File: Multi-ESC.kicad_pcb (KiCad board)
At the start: 2 copper layers, 252 parts, among them J1 Conn_01x01, J10 Conn_01x01, J11 Conn_01x01, J12 Conn_01x01, J13 Conn_01x01, J14 Conn_01x01, J15 Conn_01x01, J16 Conn_01x01, J17 Conn_01x03, J18 Conn_01x05, J2 Conn_01x01, J3 Conn_01x01, J4 Conn_01x01, J5 Conn_01x01, J6 Conn_01x01, J7 Conn_01x01, J8 Conn_01x01, J9 Conn_01x01, Q1 DI030N10PT-AQ, Q10 DI030N10PT-AQ, Q11 DI030N10PT-AQ, Q12 DI030N10PT-AQ, Q13 DI030N10PT-AQ, Q14 Q_PMOS_DGS, Q15 DI030N10PT-AQ, Q16 DI030N10PT-AQ, Q17 DI030N10PT-AQ, Q18 DI030N10PT-AQ, Q19 DI030N10PT-AQ, Q2 DI030N10PT-AQ, Q20 DI030N10PT-AQ, Q21 Q_PMOS_DGS, Q22 DI030N10PT-AQ, Q23 DI030N10PT-AQ, Q24 DI030N10PT-AQ, Q25 DI030N10PT-AQ, Q26 DI030N10PT-AQ, Q27 DI030N10PT-AQ, Q28 Q_PMOS_DGS, Q3 DI030N10PT-AQ, Q4 DI030N10PT-AQ, Q5 DI030N10PT-AQ, Q6 DI030N10PT-AQ, Q7 Q_PMOS_DGS, Q8 DI030N10PT-AQ, Q9 DI030N10PT-AQ, U1 STM32F318K8Ux, U10 DRV8320SR, U11 MIC5504-1.8YM5, U12 STM32F318K8Ux, U13 DRV8320SR, U2 DRV8320SR, U3 LMR51450FN, U4 MIC5504-1.8YM5, U5 MIC5504-1.8YM5, U6 STM32F318K8Ux, U7 DRV8320SR, U8 MIC5504-1.8YM5, U9 STM32F318K8Ux, Y1 8MHz, Y2 8MHz, Y3 8MHz, Y4 8MHz

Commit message: added journal entry
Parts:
- moved C2 5.54 mm to (260.4, 116.5), turned to -90 degrees
- moved C3 3.94 mm to (261.4, 116.5), turned to -90 degrees
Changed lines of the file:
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@@
 	(footprint "Capacitor_SMD:C_0402_1005Metric"
 		(layer "F.Cu")
-		(at 259.18 121.9)
+		(at 260.4 116.5 -90)
 		(descr "Capacitor SMD 0402 (1005 Metric), square (rectangular) end terminal, IPC-7351 nominal, (Body size source: IPC-SM-782 page 76, https://www.pcb-3d.com/wordpress/wp-content/uploads/ipc-sm-782a_amendment_1_and_2.pdf)")
 		(tags "capacitor")
 		(property "Reference" "C2"
-			(at 0 -1.16 0)
+			(at 0 -1.16 90)
 			(layer "F.SilkS")
+			(hide yes)
 			(effects
 				(font
@@
 		)
 		(property "Value" "100nF"
-			(at 0 1.16 0)
+			(at 0 1.16 90)
 			(layer "F.Fab")
 			(effects
@@
 		)
 		(property "Datasheet" ""
-			(at 0 0 0)
+			(at 0 0 90)
 			(layer "F.Fab")
 			(hide yes)
@@
 		)
 		(property "Description" "Unpolarized capacitor"
-			(at 0 0 0)
+			(at 0 0 90)
 			(layer "F.Fab")
 			(hide yes)
@@
 		)
 		(property "KiLib_Generator" "SMD_2terminal_chip_molded"
-			(at 0 0 0)
+			(at 0 0 90)
 			(layer "F.SilkS")
 			(hide yes)
@@
 		)
 		(property "MPN" ""
-			(at 0 0 0)
+			(at 0 0 270)
 			(unlocked yes)
 			(layer "F.Fab")
@@
 		(duplicate_pad_numbers_are_jumpers no)
 		(fp_line
-			(start -0.107836 -0.36)
-			(end 0.107836 -0.36)
+			(start -0.107836 0.36)
+			(end 0.107836 0.36)
 			(stroke
 				(width 0.12)
@@
 		)
 		(fp_line
-			(start -0.107836 0.36)
-			(end 0.107836 0.36)
+			(start -0.107836 -0.36)
+			(end 0.107836 -0.36)
 			(stroke
 				(width 0.12)
@@
 		)
 		(fp_text user "${REFERENCE}"
-			(at 0 0 0)
+			(at 0 0 90)
 			(layer "F.Fab")
 			(effects
@@
 		)
 		(pad "1" smd roundrect
-			(at -0.48 0)
+			(at -0.48 0 270)
 			(size 0.56 0.62)
 			(layers "F.Cu" "F.Mask" "F.Paste")
@@
 		)
 		(pad "2" smd roundrect
-			(at 0.48 0)
+			(at 0.48 0 270)
 			(size 0.56 0.62)
 			(layers "F.Cu" "F.Mask" "F.Paste")
@@
 	(footprint "Capacitor_SMD:C_0402_1005Metric"
 		(layer "F.Cu")
-		(at 259.28 119.8)
+		(at 261.4 116.48 -90)
 		(descr "Capacitor SMD 0402 (1005 Metric), square (rectangular) end terminal, IPC-7351 nominal, (Body size source: IPC-SM-782 page 76, https://www.pcb-3d.com/wordpress/wp-content/uploads/ipc-sm-782a_amendment_1_and_2.pdf)")
 		(tags "capacitor")
 		(property "Reference" "C3"
-			(at 0 -1.16 0)
+			(at 0 -1.16 90)
 			(layer "F.SilkS")
+			(hide yes)
 			(effects
 				(font
@@
 		)
 		(property "Value" "100nF"
-			(at 0 1.16 0)
+			(at 0 1.16 90)
 			(layer "F.Fab")
 			(effects
@@
 		)
 		(property "Datasheet" ""
-			(at 0 0 0)
+			(at 0 0 90)
 			(layer "F.Fab")
 			(hide yes)
@@
 		)
 		(property "Description" "Unpolarized capacitor"
-			(at 0 0 0)
+			(at 0 0 90)
 			(layer "F.Fab")
 			(hide yes)
@@
 		)
 		(property "KiLib_Generator" "SMD_2terminal_chip_molded"
-			(at 0 0 0)
+			(at 0 0 90)
 			(layer "F.SilkS")
 			(hide yes)
@@
 		)
 		(property "MPN" ""
-			(at 0 0 0)
+			(at 0 0 270)
 			(unlocked yes)
 			(layer "F.Fab")
@@
 		(duplicate_pad_numbers_are_jumpers no)
 		(fp_line
-			(start -0.107836 -0.36)
-			(end 0.107836 -0.36)
+			(start -0.107836 0.36)
+			(end 0.107836 0.36)
 			(stroke
 				(width 0.12)
@@
 		)
 		(fp_line
-			(start -0.107836 0.36)
-			(end 0.107836 0.36)
+			(start -0.107836 -0.36)
+			(end 0.107836 -0.36)
 			(stroke
 				(width 0.12)
@@
 		)
 		(fp_text user "${REFERENCE}"
-			(at 0 0 0)
+			(at 0 0 90)
 			(layer "F.Fab")
 			(effects
@@
 		)
 		(pad "1" smd roundrect
-			(at -0.48 0)
+			(at -0.48 0 270)
 			(size 0.56 0.62)
 			(layers "F.Cu" "F.Mask" "F.Paste")
@@
 		)
 		(pad "2" smd roundrect
-			(at 0.48 0)
+			(at 0.48 0 270)
 			(size 0.56 0.62)
 			(layers "F.Cu" "F.Mask" "F.Paste")

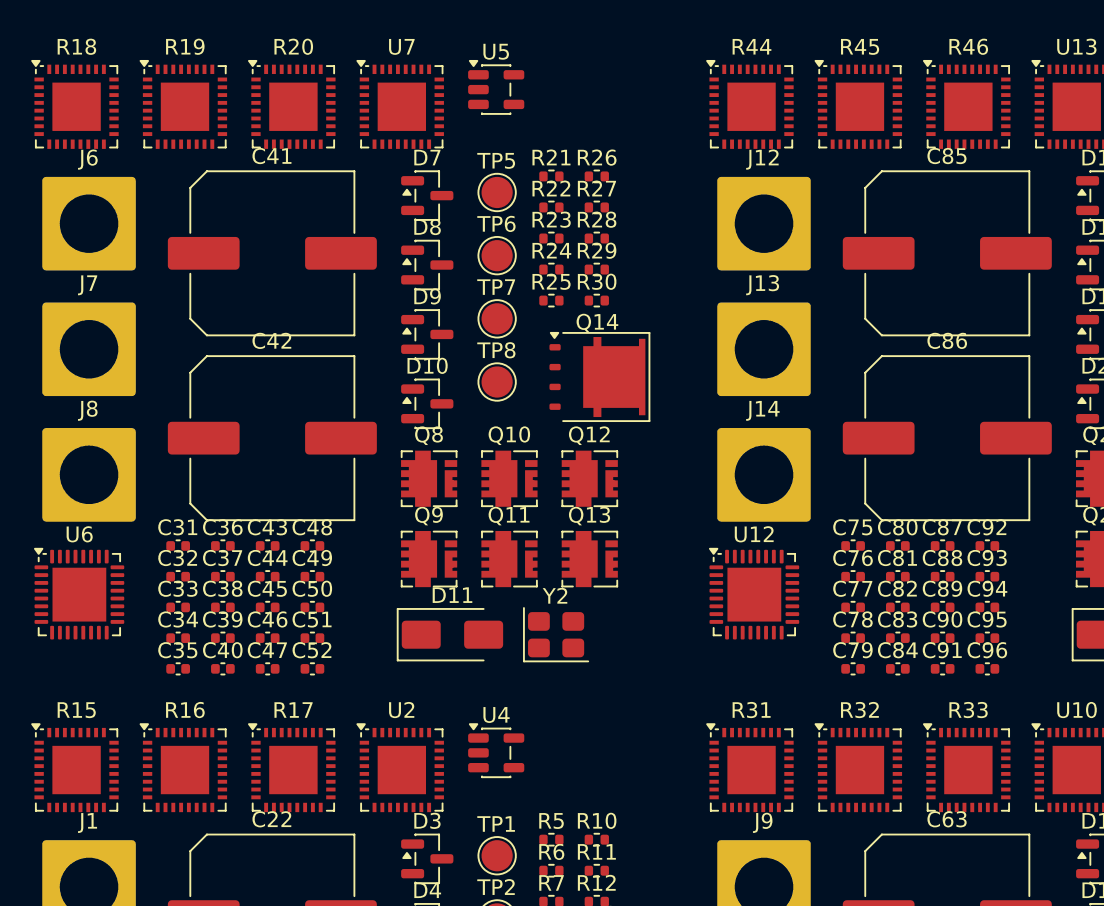
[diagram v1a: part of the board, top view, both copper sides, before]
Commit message: fixed footprints
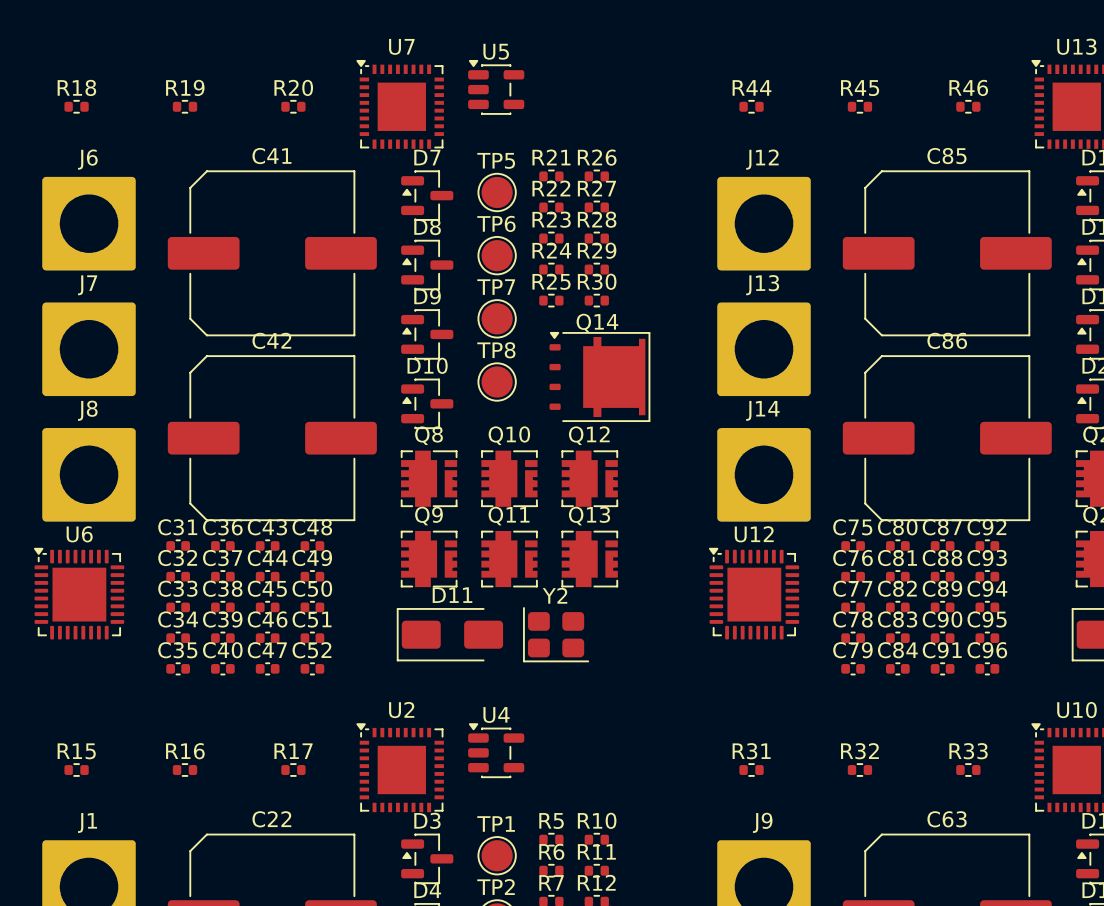
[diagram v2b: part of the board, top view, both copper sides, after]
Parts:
- R15, R16, R17, R18, R19, R20, R31, R32, R33, R44, R45, R46: footprint Package_DFN_QFN:WQFN-32-1EP_5x5mm_P0.5mm_EP3.1x3.1mm -> Resistor_SMD:R_0402_1005Metric

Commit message: set driver layout
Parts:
- removed D20, D3, D5: BAT54C, Package_TO_SOT_SMD:SOT-23
- added D23: BAT54CW, Package_TO_SOT_SMD:SOT-323_SC-70, F.Cu at (-157.3, 34.2)
- added D24: BAT54CW, Package_TO_SOT_SMD:SOT-323_SC-70, F.Cu at (-139.4, 34.2)
- added D25: BAT54CW, Package_TO_SOT_SMD:SOT-323_SC-70, F.Cu at (-145.4, 34.2)
- C24, C25, C26, C27, C28, C29, C44, C45, C47, C49, C50, C52, C66, C67, C69, C71, C72, C74, C88, C89, C91, C93, C94, C96: footprint Capacitor_SMD:C_0402_1005Metric -> Capacitor_SMD:C_1210_3225Metric
- D10, D12, D13, D14, D15, D17, D18, D19, D4, D6, D7, D8, D9: value BAT54C -> BAT54CW; footprint Package_TO_SOT_SMD:SOT-23 -> Package_TO_SOT_SMD:SOT-323_SC-70
- moved J3 253.5 mm to (88.2, 45.8)
- moved J2 253.5 mm to (88.2, 38.7)
- moved J1 253.5 mm to (88.2, 31.6)
- moved C24 238.4 mm to (82.1, 27.2)
- moved C28 236.2 mm to (82.1, 20.6)
- moved C26 235.1 mm to (82.1, 23.9)
- moved C29 231.9 mm to (77.4, 20.6), turned to 180 degrees
- moved C27 230.8 mm to (77.4, 23.9), turned to 180 degrees
- moved C25 229.8 mm to (77.4, 27.2), turned to 180 degrees
- moved U1 228.8 mm to (62.2, 38.2)
- moved Q2 227.0 mm to (82.3, 31.0), turned to 90 degrees
- moved C17 225.0 mm to (67.5, 42.6), turned to 180 degrees
- moved C9 224.9 mm to (65.0, 42.0), turned to -90 degrees
- moved C23 224.1 mm to (69.6, 25.8), turned to -90 degrees
- moved C20 223.3 mm to (69.0, 43.1), turned to -90 degrees
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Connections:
- D10 pad 1: /BLDC Driver1/VGND -> /BLDC Driver0/VGND
- D10 pad 2: Net-(C32-Pad1) -> Net-(C21-Pad1)
- D12 pad 1: /BLDC Driver2/BEMF_A -> /BLDC Driver1/BEMF_C
- D12 pad 2: /BLDC Driver2/BEMF_U_A -> /BLDC Driver1/BEMF_U_C
- D13 pad 1: /BLDC Driver2/BEMF_B -> /BLDC Driver2/BEMF_C
- D13 pad 2: /BLDC Driver2/BEMF_U_B -> /BLDC Driver2/BEMF_U_C
- D14 pad 1: /BLDC Driver2/BEMF_C -> /BLDC Driver3/BEMF_C
- D14 pad 2: /BLDC Driver2/BEMF_U_C -> /BLDC Driver3/BEMF_U_C
- D15 pad 1: /BLDC Driver2/VGND -> /BLDC Driver1/VGND
- D15 pad 2: Net-(C54-Pad1) -> Net-(C32-Pad1)
- D17 pad 1: /BLDC Driver3/BEMF_A -> /BLDC Driver3/BEMF_B
- D17 pad 2: /BLDC Driver3/BEMF_U_A -> /BLDC Driver3/BEMF_U_B
- D18 pad 1: /BLDC Driver3/BEMF_B -> /BLDC Driver2/VGND
- D18 pad 2: /BLDC Driver3/BEMF_U_B -> Net-(C54-Pad1)
- D19 pad 1: /BLDC Driver3/BEMF_C -> /BLDC Driver3/VGND
- D19 pad 2: /BLDC Driver3/BEMF_U_C -> Net-(C76-Pad1)
- D7 pad 1: /BLDC Driver1/BEMF_A -> /BLDC Driver0/BEMF_B
- D7 pad 2: /BLDC Driver1/BEMF_U_A -> /BLDC Driver0/BEMF_U_B
- D9 pad 1: /BLDC Driver1/BEMF_C -> /BLDC Driver2/BEMF_B
- D9 pad 2: /BLDC Driver1/BEMF_U_C -> /BLDC Driver2/BEMF_U_B
- R15 pad 2: Net-(R15-Pad2) -> Net-(C21-Pad1)
- R17 pad 2: Net-(R15-Pad2) -> Net-(C21-Pad1)
- R18 pad 2: Net-(R18-Pad2) -> Net-(C32-Pad1)
- R20 pad 2: Net-(R18-Pad2) -> Net-(C32-Pad1)
- R31 pad 2: Net-(R31-Pad2) -> Net-(C54-Pad1)
- R33 pad 2: Net-(R31-Pad2) -> Net-(C54-Pad1)
- R44 pad 2: Net-(R44-Pad2) -> Net-(C76-Pad1)
- R46 pad 2: Net-(R44-Pad2) -> Net-(C76-Pad1)
- U10 pad 24: (no net) -> Net-(U10-DVDD)
- U13 pad 24: (no net) -> Net-(U13-DVDD)
- U2 pad 24: (no net) -> Net-(U2-DVDD)
- U7 pad 24: (no net) -> Net-(U7-DVDD)

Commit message: made next driver layout
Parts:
- moved J6 266.9 mm to (88.1, 74.6)
- moved J7 266.6 mm to (88.1, 81.6)
- moved J8 266.3 mm to (88.1, 88.6)
- moved R18 242.8 mm to (54.1, 85.5)
- moved R25 238.7 mm to (83.3, 90.6)
- moved C50 238.5 mm to (81.9, 66.8)
- moved U6 238.4 mm to (62.6, 82.1)
- moved C52 238.3 mm to (81.9, 70.1)
- moved C49 238.2 mm to (81.9, 63.5)
- moved R26 237.6 mm to (81.3, 90.6), turned to 180 degrees
- moved R23 237.5 mm to (83.3, 83.5), turned to 180 degrees
- moved U7 237.1 mm to (69.8, 82.9), turned to 90 degrees
- moved R19 237.0 mm to (54.1, 86.5)
- moved C45 236.7 mm to (77.2, 66.8), turned to 180 degrees
- moved D15 236.7 mm to (56.2, 87.4), turned to -90 degrees
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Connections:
- R11 pad 2: /BLDC Driver0/BEMF_A -> /BLDC Driver0/BEMF_B
- R12 pad 1: /BLDC Driver0/BEMF_A -> /BLDC Driver0/BEMF_B
- R13 pad 2: /BLDC Driver0/BEMF_A -> /BLDC Driver0/BEMF_C
- R14 pad 1: /BLDC Driver0/BEMF_A -> /BLDC Driver0/BEMF_C
- R23 pad 2: /BLDC Driver1/BEMF_A -> /BLDC Driver1/BEMF_B
- R24 pad 1: /BLDC Driver1/BEMF_A -> /BLDC Driver1/BEMF_B
- R25 pad 2: /BLDC Driver1/BEMF_A -> /BLDC Driver1/BEMF_C
- R26 pad 1: /BLDC Driver1/BEMF_A -> /BLDC Driver1/BEMF_C
- R36 pad 2: /BLDC Driver2/BEMF_A -> /BLDC Driver2/BEMF_B
- R37 pad 1: /BLDC Driver2/BEMF_A -> /BLDC Driver2/BEMF_B
- R38 pad 2: /BLDC Driver2/BEMF_A -> /BLDC Driver2/BEMF_C
- R39 pad 1: /BLDC Driver2/BEMF_A -> /BLDC Driver2/BEMF_C
- R49 pad 2: /BLDC Driver3/BEMF_A -> /BLDC Driver3/BEMF_B
- R50 pad 1: /BLDC Driver3/BEMF_A -> /BLDC Driver3/BEMF_B
- R51 pad 2: /BLDC Driver3/BEMF_A -> /BLDC Driver3/BEMF_C
- R52 pad 1: /BLDC Driver3/BEMF_A -> /BLDC Driver3/BEMF_C
- U11 pad 3: unconnected-(U11-EN-Pad3) -> +3.3V
- U4 pad 3: unconnected-(U4-EN-Pad3) -> +3.3V
- U5 pad 3: unconnected-(U5-EN-Pad3) -> +3.3V
- U8 pad 3: unconnected-(U8-EN-Pad3) -> +3.3V

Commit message: routing driver
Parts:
- moved R6 0.50 mm to (71.0, 34.6), turned to -90 degrees
- moved C17 0.30 mm to (67.5, 42.9)
- moved C11 0.20 mm to (57.5, 39.5)
- moved C12 0.20 mm to (57.5, 38.5)
- turned R8 to -90 degrees
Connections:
- R10 pad 1: /BLDC Driver0/BEMF_A -> /BLDC Driver0/BEMF_U_A
- R11 pad 2: /BLDC Driver0/BEMF_B -> /BLDC Driver0/BEMF_U_B
- R12 pad 1: /BLDC Driver0/BEMF_B -> /BLDC Driver0/BEMF_U_B
- R13 pad 2: /BLDC Driver0/BEMF_C -> /BLDC Driver0/BEMF_U_C
- R14 pad 1: /BLDC Driver0/BEMF_C -> /BLDC Driver0/BEMF_U_C
- R21 pad 2: /BLDC Driver1/BEMF_A -> /BLDC Driver1/BEMF_U_A
- R22 pad 1: /BLDC Driver1/BEMF_A -> /BLDC Driver1/BEMF_U_A
- R23 pad 2: /BLDC Driver1/BEMF_B -> /BLDC Driver1/BEMF_U_B
- R24 pad 1: /BLDC Driver1/BEMF_B -> /BLDC Driver1/BEMF_U_B
- R25 pad 2: /BLDC Driver1/BEMF_C -> /BLDC Driver1/BEMF_U_C
- R26 pad 1: /BLDC Driver1/BEMF_C -> /BLDC Driver1/BEMF_U_C
- R34 pad 2: /BLDC Driver2/BEMF_A -> /BLDC Driver2/BEMF_U_A
- R35 pad 1: /BLDC Driver2/BEMF_A -> /BLDC Driver2/BEMF_U_A
- R36 pad 2: /BLDC Driver2/BEMF_B -> /BLDC Driver2/BEMF_U_B
- R37 pad 1: /BLDC Driver2/BEMF_B -> /BLDC Driver2/BEMF_U_B
- R38 pad 2: /BLDC Driver2/BEMF_C -> /BLDC Driver2/BEMF_U_C
- R39 pad 1: /BLDC Driver2/BEMF_C -> /BLDC Driver2/BEMF_U_C
- R47 pad 2: /BLDC Driver3/BEMF_A -> /BLDC Driver3/BEMF_U_A
- R48 pad 1: /BLDC Driver3/BEMF_A -> /BLDC Driver3/BEMF_U_A
- R49 pad 2: /BLDC Driver3/BEMF_B -> /BLDC Driver3/BEMF_U_B
- R50 pad 1: /BLDC Driver3/BEMF_B -> /BLDC Driver3/BEMF_U_B
- R51 pad 2: /BLDC Driver3/BEMF_C -> /BLDC Driver3/BEMF_U_C
- R52 pad 1: /BLDC Driver3/BEMF_C -> /BLDC Driver3/BEMF_U_C
- R9 pad 2: /BLDC Driver0/BEMF_A -> /BLDC Driver0/BEMF_U_A
- U1 pad 23: unconnected-(U1-PA13-Pad23) -> /BLDC Driver0/DRV_EN
- U1 pad 29: unconnected-(U1-PB6-Pad29) -> /BLDC Driver0/FAULT
- U12 pad 23: unconnected-(U12-PA13-Pad23) -> /BLDC Driver3/DRV_EN
- U12 pad 29: unconnected-(U12-PB6-Pad29) -> /BLDC Driver3/FAULT
- U6 pad 23: unconnected-(U6-PA13-Pad23) -> /BLDC Driver1/DRV_EN
- U6 pad 29: unconnected-(U6-PB6-Pad29) -> /BLDC Driver1/FAULT
- U9 pad 23: unconnected-(U9-PA13-Pad23) -> /BLDC Driver2/DRV_EN
- U9 pad 29: unconnected-(U9-PB6-Pad29) -> /BLDC Driver2/FAULT
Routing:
- net /BLDC Driver0/CS: track 0.00 -> 17.6 mm, vias 0 -> 2
- net /BLDC Driver0/FAULT: track 0.00 -> 12.9 mm, vias 0 -> 2
- net /BLDC Driver0/BEMF_U_C: track 0.00 -> 12.6 mm, vias 0 -> 2
- net /BLDC Driver0/MOSI: track 0.00 -> 11.9 mm
- net /BLDC Driver0/BEMF_U_B: track 0.00 -> 11.2 mm, vias 0 -> 2
- net /BLDC Driver0/INLC: track 0.00 -> 11.1 mm, vias 0 -> 2
- net /BLDC Driver0/MISO: track 0.00 -> 11.0 mm, vias 0 -> 2
- net /BLDC Driver0/SCLK: track 0.00 -> 9.64 mm
- net /BLDC Driver0/INHC: track 0.00 -> 8.17 mm, vias 0 -> 2
- net /BLDC Driver0/DRV_EN: track 0.00 -> 8.13 mm
- net /BLDC Driver0/BEMF_U_A: track 0.00 -> 7.96 mm, vias 0 -> 2
- net +3.3V: track 0.00 -> 7.82 mm
- net /BLDC Driver0/+1.8V: track 0.00 -> 6.74 mm, vias 0 -> 1
- net /BLDC Driver0/BEMF_A: track 0.00 -> 6.10 mm, vias 0 -> 2
- net /BLDC Driver0/HSE_OUT: track 0.00 -> 5.91 mm
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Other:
- copper layers 2 -> 4

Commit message: added zone fill
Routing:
- added copper zone on F.Cu, net VBUS
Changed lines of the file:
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@@
 		(capping no)
 		(filling no)
-		(zone_defaults)
 		(pcbplotparams
 			(layerselection 0x00000000_00000000_55555555_5755f5ff)
@@
 	)
 	(segment
-		(start 63.88 41.539386)
-		(end 63.48 41.139386)
-		(width 0.2)
-		(layer "F.Cu")
-		(net "/BLDC Driver0/BEMF_C")
-	)
-	(segment
-		(start 63.48 41.139386)
-		(end 63.48 40.6875)
-		(width 0.2)
-		(layer "F.Cu")
-		(net "/BLDC Driver0/BEMF_C")
-	)
-	(segment
-		(start 63.88 42.6125)
-		(end 63.88 41.539386)
-		(width 0.2)
-		(layer "F.Cu")
-		(net "/BLDC Driver0/BEMF_C")
-	)
-	(segment
 		(start 62.58 42.6125)
 		(end 62.58 43.42)
@@
 	)
 	(segment
-		(start 61.463695 43.463695)
-		(end 61.463695 42.656195)
+		(start 53.1275 42.3)
+		(end 53.14 42.2875)
 		(width 0.2)
 		(layer "F.Cu")
-		(net "/BLDC Driver0/BEMF_B")
+		(net "/BLDC Driver0/BEMF_U_B")
 	)
 	(segment
-		(start 62.98 41.710668)
-		(end 63.080662 41.81133)
+		(start 60.12 43.905)
+		(end 60.1 43.925)
 		(width 0.2)
 		(layer "F.Cu")
-		(net "/BLDC Driver0/BEMF_B")
+		(net "/BLDC Driver0/BEMF_U_B")
 	)
 	(segment
-		(start 61.463695 42.656195)
-		(end 61.42 42.6125)
+		(start 60.12 42.6125)
+		(end 60.12 43.905)
 		(width 0.2)
 		(layer "F.Cu")
-		(net "/BLDC Driver0/BEMF_B")
+		(net "/BLDC Driver0/BEMF_U_B")
 	)
 	(segment
-		(start 62.98 40.6875)
-		(end 62.98 41.710668)
+		(start 52.5 42.3)
+		(end 53.1275 42.3)
 		(width 0.2)
 		(layer "F.Cu")
-		(net "/BLDC Driver0/BEMF_B")
+		(net "/BLDC Driver0/BEMF_U_B")
+	)
+	(segment
+		(start 81.93 40.7)
+		(end 82.92 40.7)
+		(width 0.2)
+		(layer "F.Cu")
+		(net "/BLDC Driver0/BEMF_U_B")
 	)
 	(via
-		(at 63.080662 41.81133)
+		(at 52.5 42.3)
 		(size 0.45)
 		(drill 0.25)
 		(layers "F.Cu" "B.Cu")
-		(net "/BLDC Driver0/BEMF_B")
+		(net "/BLDC Driver0/BEMF_U_B")
 	)
 	(via
-		(at 61.463695 43.463695)
+		(at 60.1 43.925)
 		(size 0.45)
 		(drill 0.25)
 		(layers "F.Cu" "B.Cu")
-		(net "/BLDC Driver0/BEMF_B")
+		(net "/BLDC Driver0/BEMF_U_B")
 	)
 	(segment
-		(start 63.080662 41.81133)
-		(end 63.080662 41.846728)
+		(start 60.1 43.925)
+		(end 54.125 43.925)
 		(width 0.2)
 		(layer "B.Cu")
-		(net "/BLDC Driver0/BEMF_B")
+		(net "/BLDC Driver0/BEMF_U_B")
 	)
 	(segment
-		(start 63.080662 41.846728)
-		(end 61.463695 43.463695)
+		(start 54.125 43.925)
+		(end 52.5 42.3)
 		(width 0.2)
 		(layer "B.Cu")
-		(net "/BLDC Driver0/BEMF_B")
+		(net "/BLDC Driver0/BEMF_U_B")
 	)
 	(segment
@@
 	)
 	(segment
+		(start 63.88 41.539386)
+		(end 63.48 41.139386)
+		(width 0.2)
+		(layer "F.Cu")
+		(net "/BLDC Driver0/BEMF_C")
+	)
+	(segment
+		(start 63.48 41.139386)
+		(end 63.48 40.6875)
+		(width 0.2)
+		(layer "F.Cu")
+		(net "/BLDC Driver0/BEMF_C")
+	)
+	(segment
+		(start 63.88 42.6125)
+		(end 63.88 41.539386)
+		(width 0.2)
+		(layer "F.Cu")
+		(net "/BLDC Driver0/BEMF_C")
+	)
+	(segment
 		(start 65.3 38.5)
 		(end 64.6675 38.5)
@@
 	)
 	(segment
+		(start 61.463695 43.463695)
+		(end 61.463695 42.656195)
+		(width 0.2)
+		(layer "F.Cu")
+		(net "/BLDC Driver0/BEMF_B")
+	)
+	(segment
+		(start 62.98 41.710668)
+		(end 63.080662 41.81133)
+		(width 0.2)
+		(layer "F.Cu")
+		(net "/BLDC Driver0/BEMF_B")
+	)
+	(segment
+		(start 61.463695 42.656195)
+		(end 61.42 42.6125)
+		(width 0.2)
+		(layer "F.Cu")
+		(net "/BLDC Driver0/BEMF_B")
+	)
+	(segment
+		(start 62.98 40.6875)
+		(end 62.98 41.710668)
+		(width 0.2)
+		(layer "F.Cu")
+		(net "/BLDC Driver0/BEMF_B")
+	)
+	(via
+		(at 63.080662 41.81133)
+		(size 0.45)
+		(drill 0.25)
+		(layers "F.Cu" "B.Cu")
+		(net "/BLDC Driver0/BEMF_B")
+	)
+	(via
+		(at 61.463695 43.463695)
+		(size 0.45)
+		(drill 0.25)
+		(layers "F.Cu" "B.Cu")
+		(net "/BLDC Driver0/BEMF_B")
+	)
+	(segment
+		(start 63.080662 41.81133)
+		(end 63.080662 41.846728)
+		(width 0.2)
+		(layer "B.Cu")
+		(net "/BLDC Driver0/BEMF_B")
+	)
+	(segment
+		(start 63.080662 41.846728)
+		(end 61.463695 43.463695)
+		(width 0.2)
+		(layer "B.Cu")
+		(net "/BLDC Driver0/BEMF_B")
+	)
+	(segment
 		(start 65.431372 39.5)
 		(end 64.6675 39.5)
@@
 	)
 	(segment
-		(start 53.1275 42.3)
-		(end 53.14 42.2875)
-		(width 0.2)
-		(layer "F.Cu")
-		(net "/BLDC Driver0/BEMF_U_B")
-	)
-	(segment
-		(start 60.12 43.905)
-		(end 60.1 43.925)
-		(width 0.2)
-		(layer "F.Cu")
-		(net "/BLDC Driver0/BEMF_U_B")
-	)
-	(segment
-		(start 60.12 42.6125)
-		(end 60.12 43.905)
-		(width 0.2)
-		(layer "F.Cu")
-		(net "/BLDC Driver0/BEMF_U_B")
-	)
-	(segment
-		(start 52.5 42.3)
-		(end 53.1275 42.3)
-		(width 0.2)
-		(layer "F.Cu")
-		(net "/BLDC Driver0/BEMF_U_B")
-	)
-	(segment
-		(start 81.93 40.7)
-		(end 82.92 40.7)
-		(width 0.2)
-		(layer "F.Cu")
-		(net "/BLDC Driver0/BEMF_U_B")
-	)
-	(via
-		(at 52.5 42.3)
-		(size 0.45)
-		(drill 0.25)
-		(layers "F.Cu" "B.Cu")
-		(net "/BLDC Driver0/BEMF_U_B")
-	)
-	(via
-		(at 60.1 43.925)
-		(size 0.45)
-		(drill 0.25)
-		(layers "F.Cu" "B.Cu")
-		(net "/BLDC Driver0/BEMF_U_B")
-	)
-	(segment
-		(start 60.1 43.925)
-		(end 54.125 43.925)
-		(width 0.2)
-		(layer "B.Cu")
-		(net "/BLDC Driver0/BEMF_U_B")
-	)
-	(segment
-		(start 54.125 43.925)
-		(end 52.5 42.3)
-		(width 0.2)
-		(layer "B.Cu")
-		(net "/BLDC Driver0/BEMF_U_B")
-	)
-	(segment
 		(start 68.28 41.5)
 		(end 68.28 42.025)
@@
 		(net "Net-(U2-VCP)")
 	)
+	(zone
+		(net "VBUS")
+		(layer "F.Cu")
+		(hatch edge 0.5)
+		(connect_pads yes
+			(clearance 0.5)
+		)
+		(min_thickness 0.25)
+		(fill yes
+			(thermal_gap 0.5)
+			(thermal_bridge_width 0.5)
+			(island_removal_mode 0)
+		)
+		(polygon
+			(pts
+				(xy 45.3 33.8) (xy 45.3 24.9) (xy 50.5 24.9) (xy 50.5 30.4) (xy 48.2 31.6) (xy 48.2 33.8)
+			)
+		)
+	)
 	(embedded_fonts no)
